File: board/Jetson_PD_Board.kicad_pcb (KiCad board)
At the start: 4 copper layers, 23.8 x 45.5 mm, 47 parts, among them J1 USB4081-03-A, J2 768250002, Q1 NTTFS5C673NLTAG, Q2 NTTFS5C673NLTAG, Q3 NTTFS5C673NLTAG, U1 APK43070DKZ-13-FA01, U2 USBLC6-2SC6

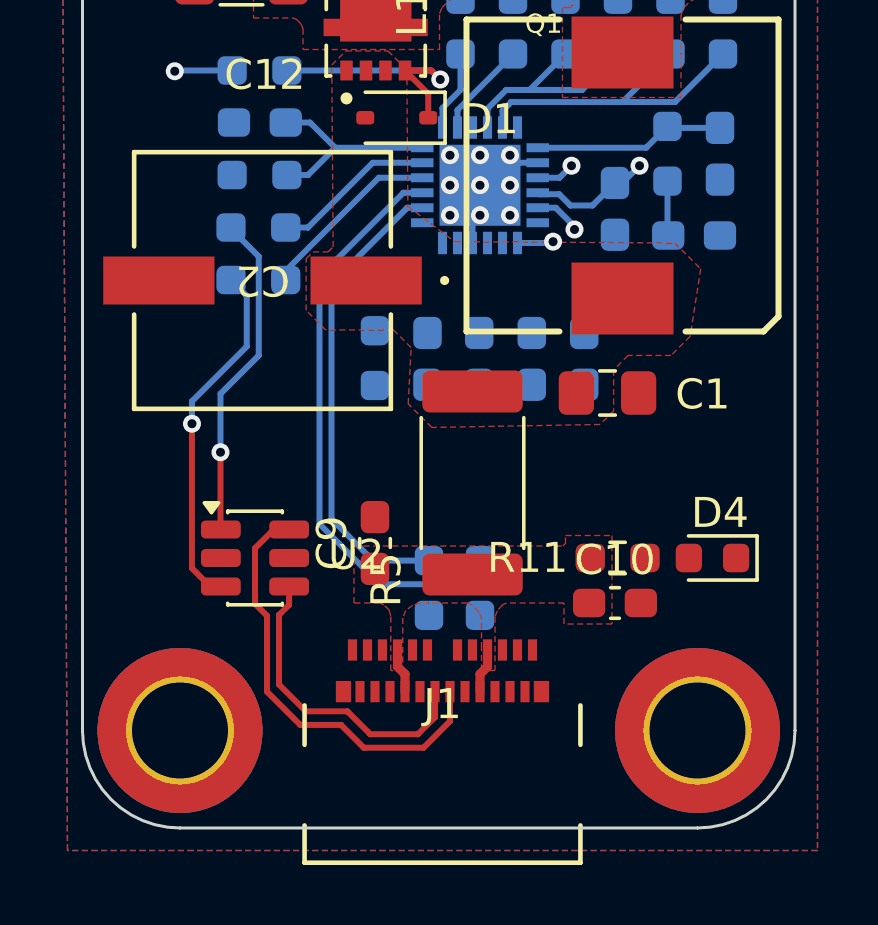
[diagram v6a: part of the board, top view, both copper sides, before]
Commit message: Connected USB-C shield to GND
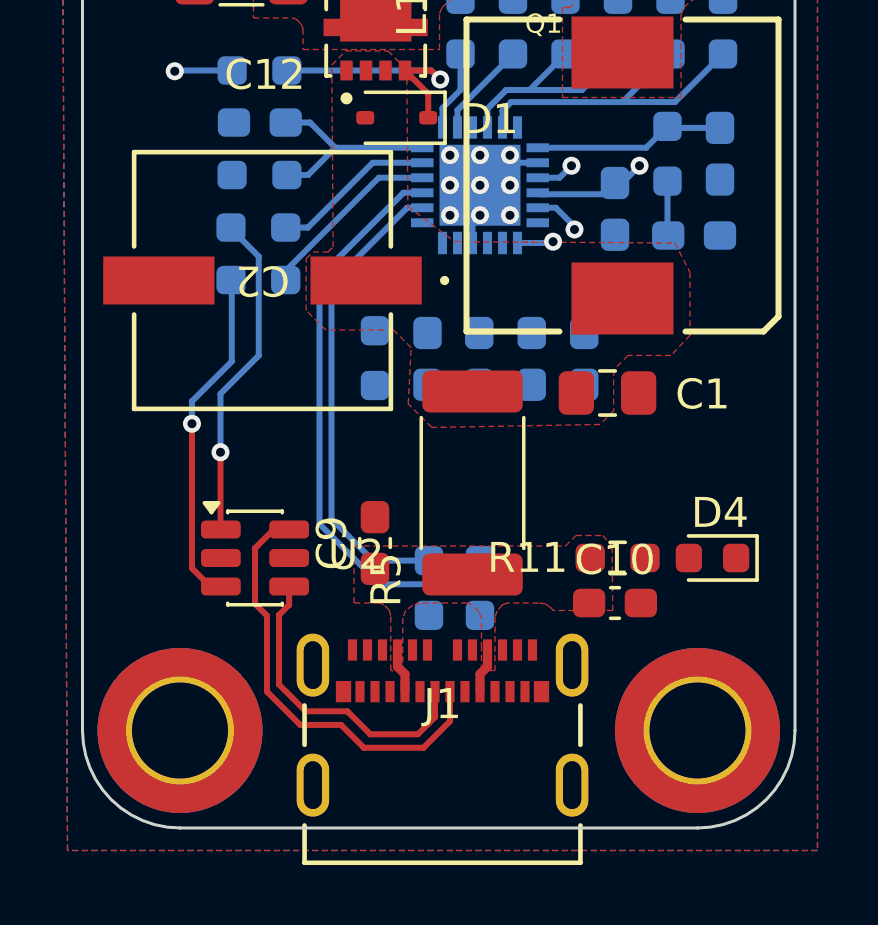
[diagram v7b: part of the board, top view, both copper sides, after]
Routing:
- net Net-(U1-GATE): track 20.5 -> 19.4 mm
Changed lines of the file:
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@@
 			(net 2 "V_{out}")
 			(pintype "passive")
+			(zone_connect 1)
 		)
 		(pad "2" smd roundrect
@@
 			)
 		)
-		(pad "" np_thru_hole oval
-			(at -4.320032 1.070608)
-			(size 1.0922 2.1082)
-			(drill oval 0.6096 1.6002)
-			(layers "*.Cu" "*.Mask")
-		)
-		(pad "" np_thru_hole oval
-			(at -4.319971 -2.929392)
-			(size 1.0922 2.1082)
-			(drill oval 0.6096 1.6002)
-			(layers "*.Cu" "*.Mask")
-		)
-		(pad "" np_thru_hole oval
-			(at 4.320032 -2.929392)
-			(size 1.0922 2.1082)
-			(drill oval 0.6096 1.6002)
-			(layers "*.Cu" "*.Mask")
-		)
-		(pad "" np_thru_hole oval
-			(at 4.320032 1.070608)
-			(size 1.0922 2.1082)
-			(drill oval 0.6096 1.6002)
-			(layers "*.Cu" "*.Mask")
-		)
 		(pad "25" smd rect
 			(at -3.299998 -2.044982)
@@
 			(net 1 "GND")
 			(pinfunction "GND")
-			(pintype "power_in")
+			(pintype "power_out")
 		)
 		(pad "A2" smd rect
@@
 			(pinfunction "SSTXN1")
 			(pintype "bidirectional+no_connect")
-			(clearance 0.1)
 		)
 		(pad "A4" smd rect
@@
 			(pinfunction "CC1")
 			(pintype "bidirectional")
-			(clearance 0.1)
 		)
 		(pad "A6" smd rect
@@
 			(pinfunction "SBU1")
 			(pintype "bidirectional+no_connect")
-			(clearance 0.1)
 		)
 		(pad "A9" smd rect
@@
 			(pinfunction "SSRXN2")
 			(pintype "bidirectional+no_connect")
-			(clearance 0.1)
 		)
 		(pad "A11" smd rect
@@
 			(net 1 "GND")
 			(pinfunction "GND")
-			(pintype "power_in")
+			(pintype "power_out")
 		)
 		(pad "B1" smd rect
@@
 			(net 1 "GND")
 			(pinfunction "GND")
-			(pintype "power_in")
+			(pintype "power_out")
 		)
 		(pad "B2" smd rect
@@
 			(net 1 "GND")
 			(pinfunction "GND")
-			(pintype "power_in")
+			(pintype "power_out")
+		)
+		(pad "SH" thru_hole oval
+			(at -4.320032 1.070608)
+			(size 1.0922 2.1082)
+			(drill oval 0.6096 1.6002)
+			(layers "*.Cu" "*.Mask")
+			(remove_unused_layers no)
+			(net 1 "GND")
+			(pinfunction "SH")
+			(pintype "input")
+		)
+		(pad "SH" thru_hole oval
+			(at -4.319971 -2.929392)
+			(size 1.0922 2.1082)
+			(drill oval 0.6096 1.6002)
+			(layers "*.Cu" "*.Mask")
+			(remove_unused_layers no)
+			(net 1 "GND")
+			(pinfunction "SH")
+			(pintype "input")
+		)
+		(pad "SH" thru_hole oval
+			(at 4.320032 -2.929392)
+			(size 1.0922 2.1082)
+			(drill oval 0.6096 1.6002)
+			(layers "*.Cu" "*.Mask")
+			(remove_unused_layers no)
+			(net 1 "GND")
+			(pinfunction "SH")
+			(pintype "input")
+		)
+		(pad "SH" thru_hole oval
+			(at 4.320032 1.070608)
+			(size 1.0922 2.1082)
+			(drill oval 0.6096 1.6002)
+			(layers "*.Cu" "*.Mask")
+			(remove_unused_layers no)
+			(net 1 "GND")
+			(pinfunction "SH")
+			(pintype "input")
 		)
 		(embedded_fonts no)
@@
 			(net 2 "V_{out}")
 			(pintype "passive")
+			(zone_connect 1)
 		)
 		(pad "2" smd roundrect
@@
 	)
 	(segment
-		(start 126.974001 93.624001)
-		(end 126.925 93.575)
+		(start 129.5 93.25)
+		(end 129.125999 93.624001)
 		(width 0.2)
 		(layer "B.Cu")
@@
 	)
 	(segment
-		(start 129.5 93.25)
-		(end 128.75 94)
+		(start 129.125999 93.624001)
+		(end 126.974001 93.624001)
 		(width 0.2)
 		(layer "B.Cu")
@@
 	)
 	(segment
-		(start 130.318506 92.674999)
-		(end 129.849663 93.143842)
+		(start 126.974001 93.624001)
+		(end 126.925 93.575)
 		(width 0.2)
 		(layer "B.Cu")
@@
 	)
 	(segment
-		(start 129.606158 93.143842)
-		(end 129.5 93.25)
+		(start 130.318506 92.674999)
+		(end 129.849663 93.143842)
 		(width 0.2)
 		(layer "B.Cu")
@@
 	)
 	(segment
-		(start 128.0171 94)
-		(end 127.641101 93.624001)
+		(start 129.606158 93.143842)
+		(end 129.5 93.25)
 		(width 0.2)
 		(layer "B.Cu")
@@
 	)
 	(segment
-		(start 127.641101 93.624001)
-		(end 126.974001 93.624001)
-		(width 0.2)
-		(layer "B.Cu")
-		(net 8)
-	)
-	(segment
-		(start 128.75 94)
-		(end 128.0171 94)
-		(width 0.2)
-		(layer "B.Cu")
-		(net 8)
-	)
-	(segment
 		(start 133.1589 81.451)
 		(end 130.674 81.451)
@@
 	)
 	(segment
-		(start 126.10279 96.55)
-		(end 124.125 96.55)
+		(start 127.42779 95.225)
+		(end 122.8 95.225)
 		(width 0.2)
 		(layer "In2.Cu")
@@
 	)
 	(segment
-		(start 114.4 89.95)
-		(end 114.825 89.525)
+		(start 118.65 91.075)
+		(end 114.725 91.075)
 		(width 0.2)
 		(layer "In2.Cu")
@@
 	)
 	(segment
-		(start 127.43569 95.2171)
-		(end 126.10279 96.55)
+		(start 127.43569 95.206237)
+		(end 127.43569 95.2171)
 		(width 0.2)
 		(layer "In2.Cu")
@@
 	)
 	(segment
-		(start 114.4 90.75)
-		(end 114.4 89.95)
+		(start 127.43569 95.2171)
+		(end 127.42779 95.225)
 		(width 0.2)
 		(layer "In2.Cu")
@@
 	)
 	(segment
-		(start 118.65 91.075)
-		(end 114.725 91.075)
+		(start 114.725 91.075)
+		(end 114.4 90.75)
 		(width 0.2)
 		(layer "In2.Cu")
@@
 	)
 	(segment
-		(start 127.43569 95.206237)
-		(end 127.43569 95.2171)
+		(start 114.4 89.95)
+		(end 114.825 89.525)
 		(width 0.2)
 		(layer "In2.Cu")
@@
 	)
 	(segment
-		(start 124.125 96.55)
-		(end 118.65 91.075)
+		(start 114.4 90.75)
+		(end 114.4 89.95)
 		(width 0.2)
 		(layer "In2.Cu")
@@
 	)
 	(segment
-		(start 114.725 91.075)
-		(end 114.4 90.75)
+		(start 122.8 95.225)
+		(end 118.65 91.075)
 		(width 0.2)
 		(layer "In2.Cu")
@@
 	)
 	(segment
-		(start 117.224 97.009399)
-		(end 116.7 96.485399)
+		(start 115.399 100.526)
+		(end 116.725 99.2)
 		(width 0.2)
 		(layer "B.Cu")
@@
 	)
 	(segment
-		(start 115.399 100.526)
-		(end 117.224 98.701)
+		(start 116.725 99.2)
+		(end 116.725 96.510399)
 		(width 0.2)
 		(layer "B.Cu")
@@
 	)
 	(segment
-		(start 117.224 98.701)
-		(end 117.224 97.009399)
+		(start 116.725 96.510399)
+		(end 116.7 96.485399)
 		(width 0.2)
 		(layer "B.Cu")
@@
 			(pts
 				(xy 120.059932 89.31711) (xy 120.525184 88.848373) (xy 121.931434 88.848373) (xy 122.561098 89.473356)
-				(xy 122.5951 94.029619) (xy 124.159329 95.207978) (xy 131.493934 95.248373) (xy 132.356434 96.110873)
-				(xy 132.006434 98.360873) (xy 131.368934 98.998373) (xy 129.934559 98.998373) (xy 129.456434 99.476498)
-				(xy 129.456434 100.842905) (xy 129.000966 101.298373) (xy 123.393934 101.398373) (xy 122.606434 100.610873)
-				(xy 122.706434 98.738998) (xy 122.115809 98.148373) (xy 119.856434 98.148373) (xy 119.206434 97.498373)
-				(xy 119.206434 95.773373) (xy 119.431434 95.548373) (xy 119.937684 95.548373) (xy 120.105175 95.379628)
+				(xy 122.5951 94.029619) (xy 124.159329 95.207978) (xy 131.493934 95.248373) (xy 132 96.225) (xy 132 98.325)
+				(xy 131.368934 98.998373) (xy 129.934559 98.998373) (xy 129.456434 99.476498) (xy 129.456434 100.842905)
+				(xy 129.000966 101.298373) (xy 123.393934 101.398373) (xy 122.606434 100.610873) (xy 122.706434 98.738998)
+				(xy 122.115809 98.148373) (xy 119.856434 98.148373) (xy 119.206434 97.498373) (xy 119.206434 95.773373)
+				(xy 119.431434 95.548373) (xy 119.937684 95.548373) (xy 120.105175 95.379628)
 			)
 		)
@@
 		(polygon
 			(pts
-				(xy 129.4 105) (xy 129.4 107.95) (xy 127.8 107.95) (xy 127.8 107.25) (xy 125.886433 107.25) (xy 125.74375 107.315625)
-				(xy 125.575 107.5125) (xy 125.5 107.715244) (xy 125.5 109.5) (xy 125.05 109.5) (xy 125.05 108.75)
-				(xy 125.05 107.757582) (xy 124.95625 107.53125) (xy 124.745313 107.320313) (xy 124.575563 107.25)
-				(xy 123.007582 107.25) (xy 122.75625 107.325) (xy 122.525 107.5) (xy 122.425 107.749437) (xy 122.425 109.525)
-				(xy 122.025 109.5) (xy 122.025 107.672985) (xy 121.971875 107.484375) (xy 121.796094 107.308594)
-				(xy 121.654636 107.25) (xy 120.8 107.25) (xy 120.8 105.35) (xy 127.7625 105.35) (xy 127.85 105.2625)
-				(xy 127.85 105)
+				(xy 129.1 105) (xy 129.403762 105.387482) (xy 129.425 107.5) (xy 127.45 107.5) (xy 127.35 107.4)
+				(xy 127.175 107.275) (xy 126.95 107.25) (xy 125.886433 107.25) (xy 125.74375 107.315625) (xy 125.575 107.5125)
+				(xy 125.5 107.715244) (xy 125.5 109.5) (xy 125.05 109.5) (xy 125.05 108.75) (xy 125.05 107.757582)
+				(xy 124.95625 107.53125) (xy 124.745313 107.320313) (xy 124.575563 107.25) (xy 123.007582 107.25)
+				(xy 122.75625 107.325) (xy 122.525 107.5) (xy 122.425 107.749437) (xy 122.425 109.525) (xy 122.025 109.5)
+				(xy 122.025 107.672985) (xy 121.971875 107.484375) (xy 121.796094 107.308594) (xy 121.654636 107.25)
+				(xy 120.8 107.25) (xy 120.8 105.35) (xy 127.85 105.35) (xy 128.2 105)
 			)
 		)

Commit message: Finished routing before DRC
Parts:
- moved C14 4.92 mm to (118.5, 100.2)
- moved R3 1.90 mm to (123.4, 99.0)
- moved C5 0.14 mm to (128.6, 99.0)
- moved C7 0.14 mm to (125.0, 99.0)
- moved C8 0.14 mm to (126.8, 99.0)
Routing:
- net V_{batt}: track 0.00 -> 18.5 mm, vias 0 -> 2
- net V5V: track 0.00 -> 16.4 mm, vias 0 -> 2
- net V_{out}: track 2.98 -> 17.2 mm, vias 0 -> 1
- net /Buck_{out}: track 0.00 -> 12.8 mm, vias 0 -> 1
- net Net-(U1-VFB): track 0.00 -> 8.78 mm, vias 0 -> 2
- net Net-(C5-Pad1): track 0.00 -> 5.87 mm
- net CC1: track 0.00 -> 5.38 mm, vias 0 -> 1
- net CC2: track 0.00 -> 4.84 mm, vias 0 -> 1
- net Net-(U1-VDRV): track 0.00 -> 3.32 mm
- net Net-(D5-A): track 0.00 -> 3.08 mm
- net Net-(U1-BST): track 0.00 -> 2.74 mm
- net Net-(D4-A): track 0.00 -> 1.46 mm
- net Net-(U1-GATE): track 19.4 -> 18.5 mm
- net Net-(Q1-G): track 27.5 -> 27.0 mm
